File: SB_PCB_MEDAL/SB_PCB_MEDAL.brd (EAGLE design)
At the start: 60 x 60 mm, 10 parts, among them IC1 ATTINY44A-SSU

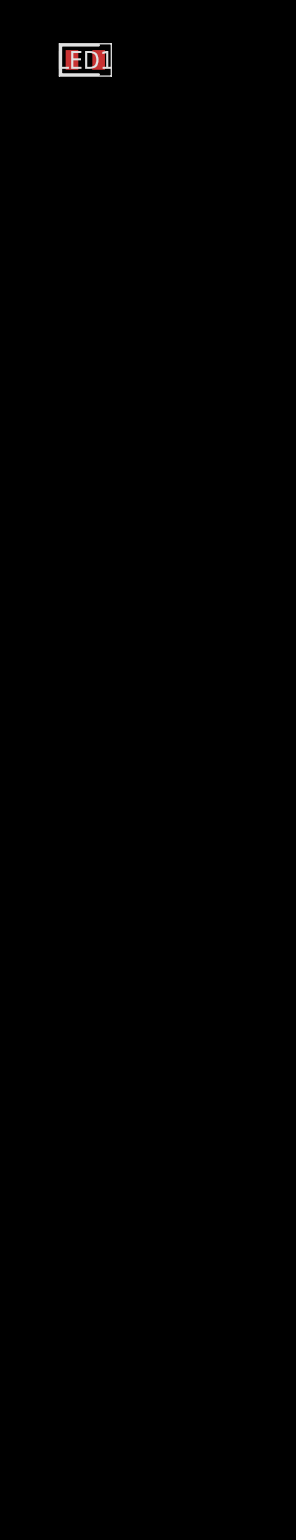
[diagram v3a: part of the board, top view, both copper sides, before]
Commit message: completed circuit for charliplexed LEDs
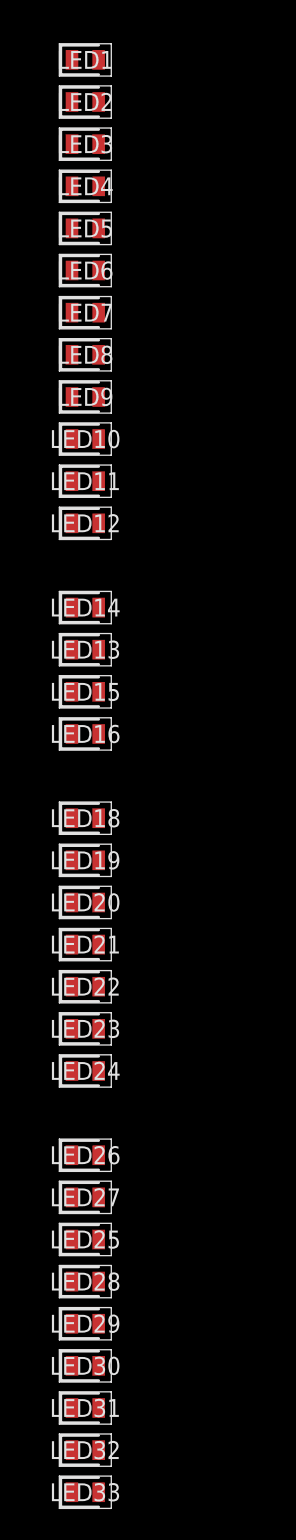
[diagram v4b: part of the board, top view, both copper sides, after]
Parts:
- added LED10, LED11, LED12, LED13, LED14, LED15, LED16, LED18, LED19, LED2, LED20, LED21, LED22, LED23, LED24, LED25, LED26, LED27, LED28, LED29, LED3, LED30, LED31, LED32, LED33, LED4, LED5, LED6, LED7, LED8, LED9: KPT-2012CGCK, SamacSys_Parts:LEDC2012X78N
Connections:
- new net N$1: LED26.2
- new net N$10: LED2.2, LED4.1
- new net N$2: LED3.1, LED5.2, LED7.2
- new net N$3: LED1.1, LED3.2
- new net N$4: LED5.1, LED7.1, LED8.2, LED9.2
- new net N$5: LED11.2, LED8.1, LED9.1
- new net N$6: LED10.2, LED12.1
- new net N$7: LED10.1, LED6.2
- new net N$8: LED4.2, LED6.1

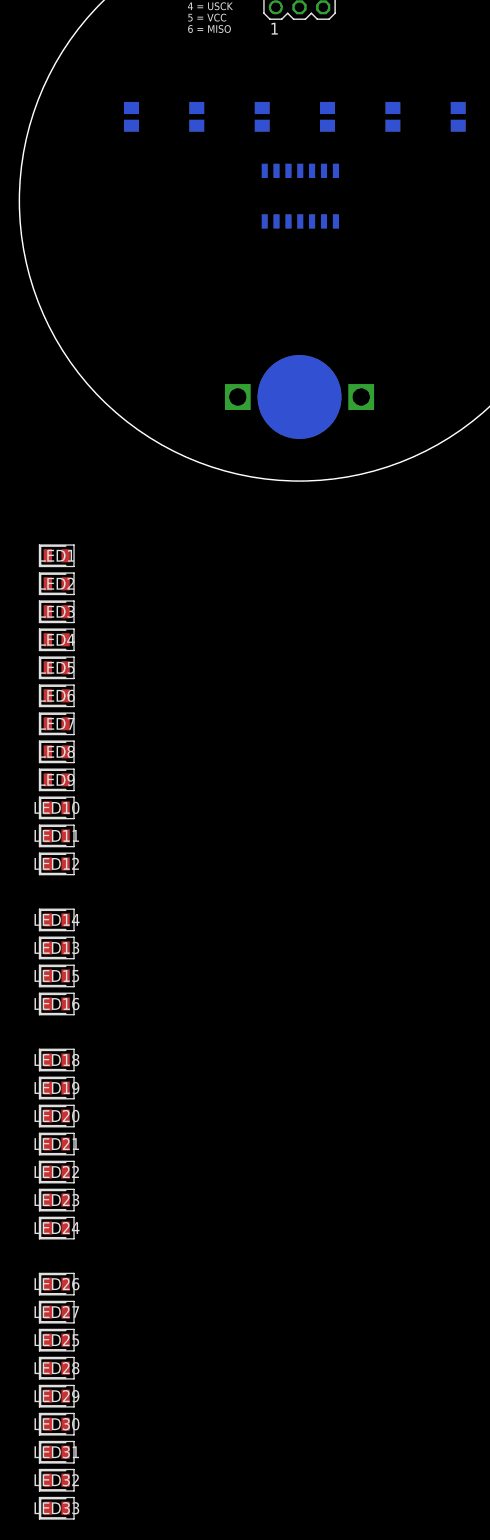
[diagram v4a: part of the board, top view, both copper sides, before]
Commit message: re-did some wiring
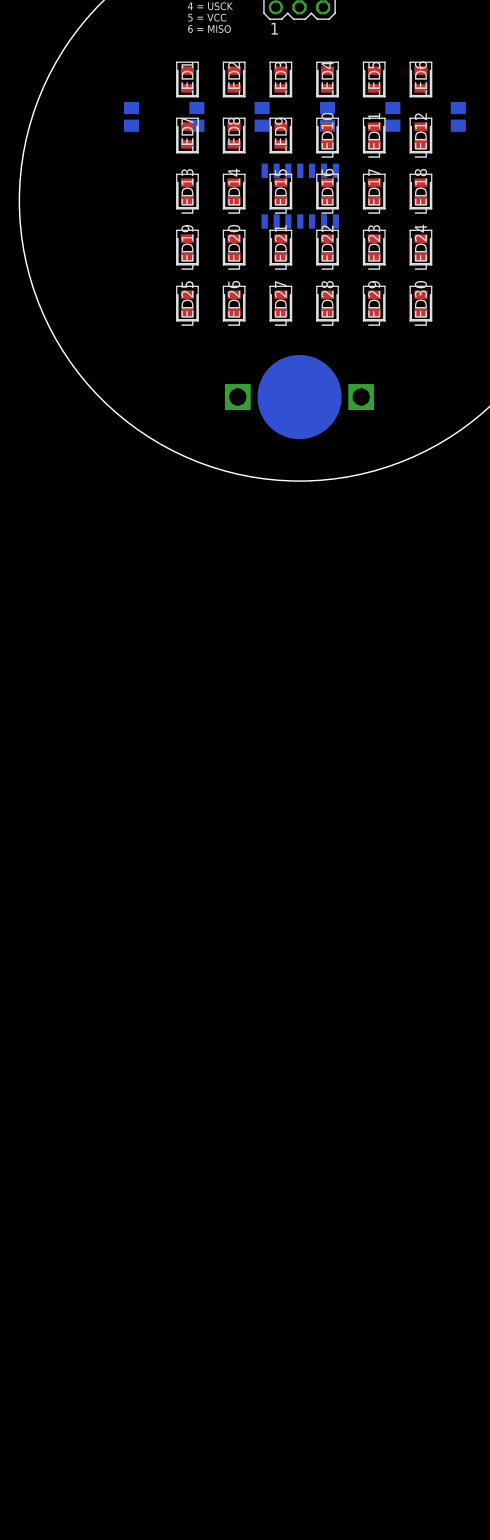
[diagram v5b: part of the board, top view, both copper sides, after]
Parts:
- removed LED31, LED32, LED33: KPT-2012CGCK, SamacSys_Parts:LEDC2012X78N
- added LED17: KPT-2012CGCK, SamacSys_Parts:LEDC2012X78N
- moved LED30 126.2 mm to (13.0, -11.0), turned to 90 degrees
- moved LED29 121.8 mm to (8.00, -11.0), turned to 90 degrees
- moved LED28 117.6 mm to (3.00, -11.0), turned to 90 degrees
- moved LED24 112.0 mm to (13.0, -5.00), turned to 90 degrees
- moved LED25 111.9 mm to (-12.0, -11.0), turned to 90 degrees
- moved LED27 110.6 mm to (-2.00, -11.0), turned to 90 degrees
- moved LED23 107.5 mm to (8.00, -5.00), turned to 90 degrees
- moved LED26 106.7 mm to (-7.00, -11.0), turned to 90 degrees
- moved LED22 103.2 mm to (3.00, -5.00), turned to 90 degrees
- moved LED18 100.8 mm to (13.0, 1.00), turned to 90 degrees
- moved LED21 99.0 mm to (-2.00, -5.00), turned to 90 degrees
- moved LED20 94.9 mm to (-7.00, -5.00), turned to 90 degrees
- moved LED16 91.7 mm to (3.00, 1.00), turned to 90 degrees
- moved LED19 91.1 mm to (-12.0, -5.00), turned to 90 degrees
- moved LED15 87.4 mm to (-2.00, 1.00), turned to 90 degrees
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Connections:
- removed net N$10: LED2.2, LED4.1
- removed net N$7: LED10.1, LED6.2
- removed net N$8: LED4.2, LED6.1
- net N$1: now also LED1.2, LED11.2, LED12.1, LED19.2, LED2.1, LED20.1, LED25.2, LED26.1, LED29.2, LED30.1, R1.2; no longer LED26.2
- net N$2: now also LED1.1, LED13.2, LED14.1, LED2.2, LED21.2, LED22.1, LED27.2, LED28.1, LED3.2, LED4.1, R2.2; no longer LED3.1, LED5.2, LED7.2
- net N$3: now also LED11.1, LED12.2, LED15.2, LED16.1, LED23.2, LED24.1, LED3.1, LED4.2, LED5.2, LED6.1, R3.2; no longer LED1.1, LED3.2
- net N$4: now also LED13.1, LED14.2, LED17.2, LED18.1, LED19.1, LED20.2, LED6.2, LED7.2, LED8.1, R4.2; no longer LED7.1, LED8.2, LED9.2
- net N$5: now also LED10.1, LED15.1, LED16.2, LED21.1, LED22.2, LED25.1, LED26.2, LED7.1, LED8.2, LED9.2, R5.2; no longer LED11.2, LED8.1, LED9.1
- net N$6: now also LED17.1, LED18.2, LED23.1, LED24.2, LED27.1, LED28.2, LED29.1, LED30.2, LED9.1, R6.2; no longer LED12.1

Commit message: added labels to pins
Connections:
- new net N$19: IC1.5
- new net N$20: IC1.6
- new net PA0: IC1.13, R1.1
- new net PA1: IC1.12, R2.1
- new net PA2: IC1.11, R3.1
- new net PA3: IC1.10, R4.1
- new net PB0: IC1.2, R5.1
- new net PB1: IC1.3, R6.1
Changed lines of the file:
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@@
 <?xml version="1.0" encoding="utf-8"?>
 <!DOCTYPE eagle SYSTEM "eagle.dtd">
-<eagle version="8.3.1">
+<eagle version="8.4.3">
 <drawing>
 <settings>
@@
 <param name="dpMaxLengthDifference" value="10mm"/>
 <param name="dpGapFactor" value="2.5"/>
-<param name="checkGrid" value="0"/>
 <param name="checkAngle" value="0"/>
 <param name="checkFont" value="1"/>
 <param name="checkRestrict" value="1"/>
+<param name="checkStop" value="0"/>
 <param name="useDiameter" value="13"/>
 <param name="maxErrors" value="50"/>
@@
 <wire x1="17" y1="9.95" x2="-2" y2="6.05" width="0" layer="19" extent="1-16"/>
 </signal>
+<signal name="PA0">
+<contactref element="IC1" pad="13"/>
+<contactref element="R1" pad="1"/>
+<wire x1="-2.46" y1="-2.201" x2="-18" y2="8.05" width="0" layer="19" extent="16-16"/>
+</signal>
+<signal name="PA1">
+<contactref element="IC1" pad="12"/>
+<contactref element="R2" pad="1"/>
+<wire x1="-1.19" y1="-2.201" x2="-11" y2="8.05" width="0" layer="19" extent="16-16"/>
+</signal>
+<signal name="PA2">
+<contactref element="IC1" pad="11"/>
+<contactref element="R3" pad="1"/>
+<wire x1="0.08" y1="-2.201" x2="-4" y2="8.05" width="0" layer="19" extent="16-16"/>
+</signal>
+<signal name="PA3">
+<contactref element="IC1" pad="10"/>
+<contactref element="R4" pad="1"/>
+<wire x1="1.35" y1="-2.201" x2="3" y2="8.05" width="0" layer="19" extent="16-16"/>
+</signal>
+<signal name="PB0">
+<contactref element="IC1" pad="2"/>
+<contactref element="R5" pad="1"/>
+<wire x1="-2.46" y1="3.221" x2="10" y2="8.05" width="0" layer="19" extent="16-16"/>
+</signal>
+<signal name="PB1">
+<contactref element="IC1" pad="3"/>
+<contactref element="R6" pad="1"/>
+<wire x1="-1.19" y1="3.221" x2="17" y2="8.05" width="0" layer="19" extent="16-16"/>
+</signal>
+<signal name="N$19">
+<contactref element="IC1" pad="5"/>
+</signal>
+<signal name="N$20">
+<contactref element="IC1" pad="6"/>
+</signal>
 </signals>

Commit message: modify board
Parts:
- removed IC1: ATTINY44A-SSU, SamacSys_Parts:SOIC127P600X175-14N
- added U1: ATMEGA16U2-AU, Atmel_By_element14_Batch_1-00:QFP80P900X900X120-32N
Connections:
- removed net N$19: IC1.5
- removed net N$20: IC1.6
- new net AVCC: U1.32
- new net UVCC: U1.31
- net GND: no longer IC1.14
- net MISO: no longer IC1.8
- net MOSI: no longer IC1.7
- net PA0: no longer IC1.13
- net PA1: no longer IC1.12
- net PA2: no longer IC1.11
- net PA3: no longer IC1.10
- net PB0: no longer IC1.2
- net PB1: no longer IC1.3
- net RST: no longer IC1.4
- net USCK: no longer IC1.9
- net VCC: now also U1.4; no longer IC1.1
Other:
- board size 60 x 60 mm -> 90 x 90 mm
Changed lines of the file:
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@@
 <?xml version="1.0" encoding="utf-8"?>
 <!DOCTYPE eagle SYSTEM "eagle.dtd">
-<eagle version="8.4.3">
+<eagle version="8.6.0">
 <drawing>
 <settings>
@@
 <layer number="59" name="tCarbon" color="7" fill="1" visible="no" active="no"/>
 <layer number="60" name="bCarbon" color="7" fill="1" visible="no" active="no"/>
+<layer number="88" name="SimResults" color="9" fill="1" visible="no" active="no"/>
+<layer number="89" name="SimProbes" color="9" fill="1" visible="no" active="no"/>
 <layer number="90" name="Modules" color="5" fill="1" visible="no" active="no"/>
 <layer number="91" name="Nets" color="2" fill="1" visible="no" active="no"/>
@@
 <board>
 <plain>
-<circle x="0" y="0" radius="30" width="0.1524" layer="20"/>
+<circle x="0" y="0" radius="45" width="0.1524" layer="20"/>
 <text x="-12" y="18" size="0.8128" layer="25">1 = GND
 2 = RST
@@
 <param name="checkRestrict" value="1"/>
 <param name="checkStop" value="0"/>
+<param name="checkValues" value="0"/>
 <param name="useDiameter" value="13"/>
 <param name="maxErrors" value="50"/>
@@
 </autorouter>
 <elements>
-<element name="IC1" library="SamacSys_Parts" package="SOIC127P600X175-14N" value="ATTINY44A-SSU" x="0.08" y="0.51" rot="MR270">
-<attribute name="3D_PACKAGE" value="" x="0.08" y="0.51" size="1.778" layer="28" rot="MR270" display="off"/>
-<attribute name="ALLIED_NUMBER" value="" x="0.08" y="0.51" size="1.778" layer="28" rot="MR270" display="off"/>
-<attribute name="DESCRIPTION" value="ATTINY44A-SSU, 8 bit AVR Microcontroller 20MHz 256 B, 4 kB Flash, 256 B RAM, I2C 14-Pin SOIC" x="0.08" y="0.51" size="1.778" layer="28" rot="MR270" display="off"/>
-<attribute name="HEIGHT" value="1.75mm" x="0.08" y="0.51" size="1.778" layer="28" rot="MR270" display="off"/>
-<attribute name="MANUFACTURER_NAME" value="Microchip" x="0.08" y="0.51" size="1.778" layer="28" rot="MR270" display="off"/>
-<attribute name="MANUFACTURER_PART_NUMBER" value="ATTINY44A-SSU" x="0.08" y="0.51" size="1.778" layer="28" rot="MR270" display="off"/>
-<attribute name="OTHER_PART_NUMBER" value="" x="0.08" y="0.51" size="1.778" layer="28" rot="MR270" display="off"/>
-<attribute name="RS_PART_NUMBER" value="1331640P" x="0.08" y="0.51" size="1.778" layer="28" rot="MR270" display="off"/>
-<attribute name="SUPPLIER_NAME" value="RS" x="0.08" y="0.51" size="1.778" layer="28" rot="MR270" display="off"/>
-</element>
 <element name="R1" library="resistor" package="M0805" value="10 Ω" x="-18" y="9" rot="MR90"/>
 <element name="R2" library="resistor" package="M0805" value="10 Ω" x="-11" y="9" rot="MR90"/>
@@
 <attribute name="SUPPLIER_NAME" value="RS" x="13" y="-11" size="1.778" layer="27" rot="R90" display="off"/>
 </element>
+<element name="U1" library="Atmel_By_element14_Batch_1-00" package="QFP80P900X900X120-32N" value="ATMEGA16U2-AU" x="-54" y="-36">
+<attribute name="MPN" value="ATMEGA16U2-AU" x="-54" y="-36" size="1.778" layer="27" display="off"/>
+<attribute name="OC_FARNELL" value="1841607" x="-54" y="-36" size="1.778" layer="27" display="off"/>
+<attribute name="OC_NEWARK" value="12T1292" x="-54" y="-36" size="1.778" layer="27" display="off"/>
+<attribute name="PACKAGE" value="QFP-32" x="-54" y="-36" size="1.778" layer="27" display="off"/>
+<attribute name="SUPPLIER" value="Atmel" x="-54" y="-36" size="1.778" layer="27" display="off"/>
+</element>
 </elements>
 <signals>
 <signal name="VCC">
-<contactref element="IC1" pad="1"/>
 <contactref element="ICSP" pad="5"/>
 <contactref element="BT1" pad="VCC@1"/>
-<wire x1="-3.73" y1="3.221" x2="-6.604" y2="-21" width="0" layer="19" extent="16-16"/>
-<wire x1="2.54" y1="20.73" x2="-3.73" y2="3.221" width="0" layer="19" extent="16-16"/>
+<contactref element="U1" pad="4"/>
+<wire x1="-6.604" y1="-21" x2="-58.1148" y2="-35.5936" width="0" layer="19" extent="1-1"/>
+<wire x1="2.54" y1="20.73" x2="-6.604" y2="-21" width="0" layer="19" extent="1-1"/>
 </signal>
 <signal name="GND">
 <contactref element="ICSP" pad="1"/>
-<contactref element="IC1" pad="14"/>
 <contactref element="BT1" pad="GND"/>
-<wire x1="-3.73" y1="-2.201" x2="0" y2="-21" width="0" layer="19" extent="1-16"/>
-<wire x1="-2.54" y1="20.73" x2="-3.73" y2="-2.201" width="0" layer="19" extent="16-16"/>
+<wire x1="-2.54" y1="20.73" x2="0" y2="-21" width="0" layer="19" extent="16-16"/>
 </signal>
 <signal name="MISO">
 <contactref element="ICSP" pad="6"/>
-<contactref element="IC1" pad="8"/>
-<wire x1="3.89" y1="-2.201" x2="2.54" y2="23.27" width="0" layer="19" extent="16-16"/>
 </signal>
 <signal name="MOSI">
-<contactref element="IC1" pad="7"/>
 <contactref element="ICSP" pad="3"/>
-<wire x1="3.89" y1="3.221" x2="0" y2="20.73" width="0" layer="19" extent="16-16"/>
 </signal>
 <signal name="RST">
-<contactref element="IC1" pad="4"/>
 <contactref element="ICSP" pad="2"/>
-<wire x1="0.08" y1="3.221" x2="-2.54" y2="23.27" width="0" layer="19" extent="16-16"/>
 </signal>
 <signal name="USCK">
-<contactref element="IC1" pad="9"/>
 <contactref element="ICSP" pad="4"/>
-<wire x1="2.62" y1="-2.201" x2="0" y2="23.27" width="0" layer="19" extent="16-16"/>
 </signal>
 <signal name="N$1">
@@
 </signal>
 <signal name="PA0">
-<contactref element="IC1" pad="13"/>
 <contactref element="R1" pad="1"/>
-<wire x1="-2.46" y1="-2.201" x2="-18" y2="8.05" width="0" layer="19" extent="16-16"/>
 </signal>
 <signal name="PA1">
-<contactref element="IC1" pad="12"/>
 <contactref element="R2" pad="1"/>
-<wire x1="-1.19" y1="-2.201" x2="-11" y2="8.05" width="0" layer="19" extent="16-16"/>
 </signal>
 <signal name="PA2">
-<contactref element="IC1" pad="11"/>
 <contactref element="R3" pad="1"/>
-<wire x1="0.08" y1="-2.201" x2="-4" y2="8.05" width="0" layer="19" extent="16-16"/>
 </signal>
 <signal name="PA3">
-<contactref element="IC1" pad="10"/>
 <contactref element="R4" pad="1"/>
-<wire x1="1.35" y1="-2.201" x2="3" y2="8.05" width="0" layer="19" extent="16-16"/>
 </signal>
 <signal name="PB0">
-<contactref element="IC1" pad="2"/>
 <contactref element="R5" pad="1"/>
-<wire x1="-2.46" y1="3.221" x2="10" y2="8.05" width="0" layer="19" extent="16-16"/>
 </signal>
 <signal name="PB1">
-<contactref element="IC1" pad="3"/>
 <contactref element="R6" pad="1"/>
-<wire x1="-1.19" y1="3.221" x2="17" y2="8.05" width="0" layer="19" extent="16-16"/>
-</signal>
-<signal name="N$19">
-<contactref element="IC1" pad="5"/>
-</signal>
-<signal name="N$20">
-<contactref element="IC1" pad="6"/>
+</signal>
+<signal name="UVCC">
+<contactref element="U1" pad="31"/>
+</signal>
+<signal name="AVCC">
+<contactref element="U1" pad="32"/>
 </signal>
 </signals>
